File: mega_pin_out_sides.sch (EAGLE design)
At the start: 101 parts, among them T1 2N2222, T10 2N2222, T11 2N2222, T12 2N2222, T13 2N2222, T14 2N2222, T15 2N2222, T16 2N2222, T17 2N2222, T18 2N2222, T2 2N2222, T3 2N2222, T4 2N2222, T5 2N2222, T6 2N2222, T7 2N2222, T8 2N2222, T9 2N2222

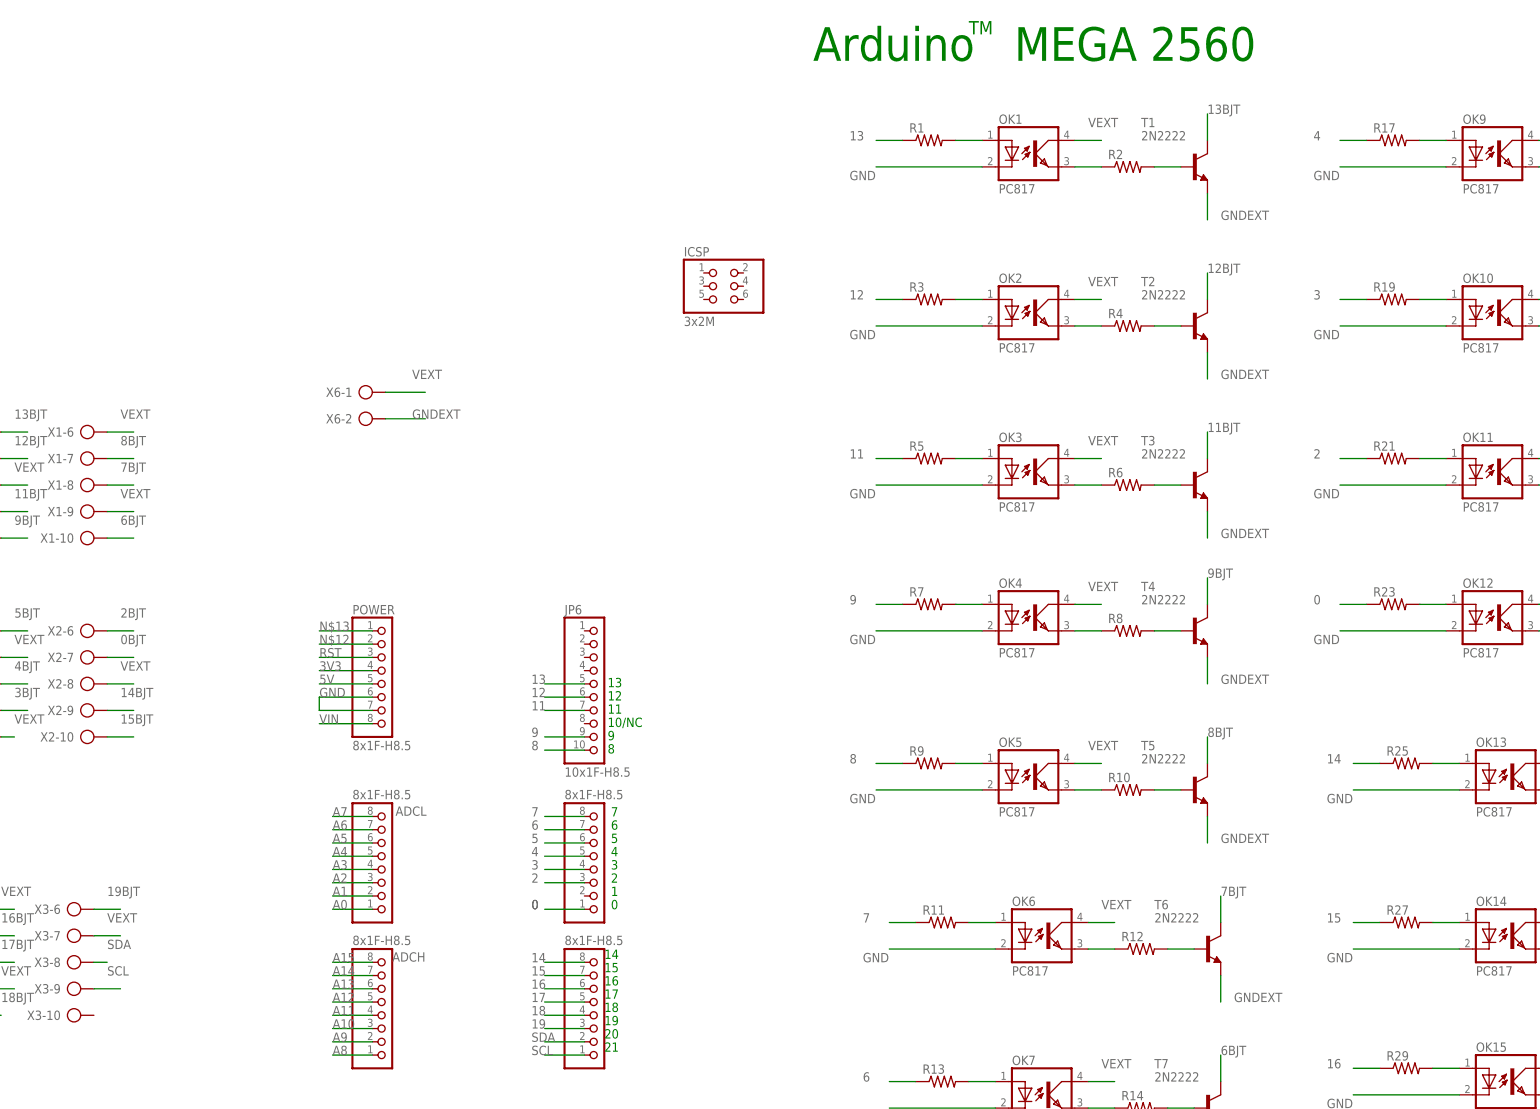
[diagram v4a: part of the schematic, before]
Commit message: [SIDES] Added header jumper pins for Flashing
- During Flashing or Reset Pin 13, 9 & 0 flashes several times and this will trigger the relays. A header jumper to be removed during flashing and after start up they are back again in place.
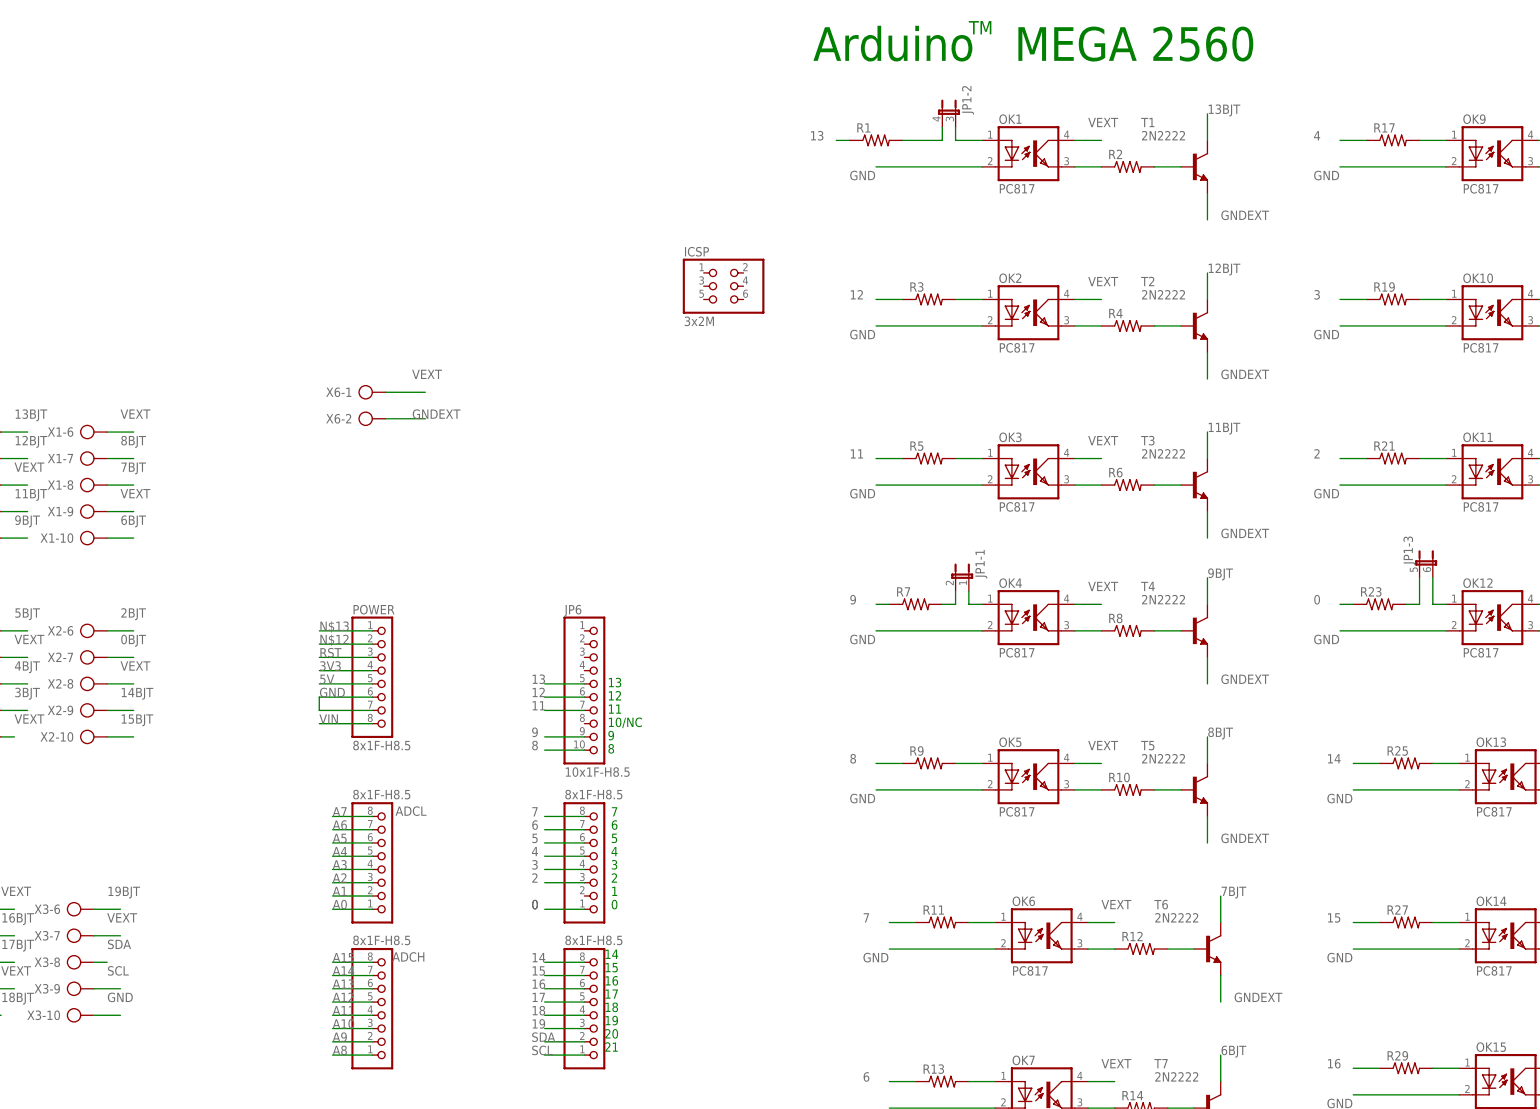
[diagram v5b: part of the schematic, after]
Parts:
- added JP1: (no value), jumper:JP3QE
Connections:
- new net N$10: JP1-3.2, OK12.A
- new net N$11: JP1-1.1, OK4.A
- new net N$9: JP1-2.1, OK1.A
- net GND: now also X3-10.KL
- net N$1: now also JP1-2.2; no longer OK1.A
- net N$19: now also JP1-1.2; no longer OK4.A
- net N$44: now also JP1-3.1; no longer OK12.A
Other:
- moved on the sheet: R1, R23, R7
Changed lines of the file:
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@@
 <part name="C15" library="adafruit" deviceset="CPOL-US" device="E2-4"/>
 <part name="C16" library="adafruit" deviceset="CPOL-US" device="E2-4"/>
+<part name="JP1" library="jumper" deviceset="JP3QE" device=""/>
 </parts>
 <sheets>
@@
 <instance part="X5" gate="-9" x="71.12" y="-121.92"/>
 <instance part="X5" gate="-10" x="76.2" y="-144.78"/>
-<instance part="R1" gate="G$1" x="127" y="165.1"/>
+<instance part="R1" gate="G$1" x="116.84" y="165.1"/>
 <instance part="OK1" gate="A" x="147.32" y="162.56"/>
 <instance part="R2" gate="G$1" x="165.1" y="160.02"/>
@@
 <instance part="R6" gate="G$1" x="165.1" y="99.06"/>
 <instance part="T3" gate="G$1" x="177.8" y="99.06"/>
-<instance part="R7" gate="G$1" x="127" y="76.2"/>
+<instance part="R7" gate="G$1" x="124.46" y="76.2"/>
 <instance part="OK4" gate="A" x="147.32" y="73.66"/>
 <instance part="R8" gate="G$1" x="165.1" y="71.12"/>
@@
 <instance part="R32" gate="G$1" x="256.54" y="-48.26"/>
 <instance part="T16" gate="G$1" x="269.24" y="-48.26"/>
-<instance part="R23" gate="G$1" x="215.9" y="76.2"/>
+<instance part="R23" gate="G$1" x="213.36" y="76.2"/>
 <instance part="OK12" gate="A" x="236.22" y="73.66"/>
 <instance part="R24" gate="G$1" x="254" y="71.12"/>
@@
 <instance part="C15" gate="G$1" x="83.82" y="-129.54"/>
 <instance part="C16" gate="G$1" x="83.82" y="-152.4"/>
+<instance part="JP1" gate="-1" x="134.62" y="81.28" rot="MR0"/>
+<instance part="JP1" gate="-2" x="132.08" y="170.18" rot="MR0"/>
+<instance part="JP1" gate="-3" x="220.98" y="83.82"/>
 </instances>
 <busses>
@@
 <segment>
 <pinref part="R1" gate="G$1" pin="2"/>
-<pinref part="OK1" gate="A" pin="A"/>
-<wire x1="132.08" y1="165.1" x2="137.16" y2="165.1" width="0.1524" layer="91"/>
+<wire x1="121.92" y1="165.1" x2="129.54" y2="165.1" width="0.1524" layer="91"/>
+<pinref part="JP1" gate="-2" pin="2"/>
+<wire x1="129.54" y1="165.1" x2="129.54" y2="167.64" width="0.1524" layer="91"/>
 </segment>
 </net>
@@
 <segment>
 <pinref part="R1" gate="G$1" pin="1"/>
-<wire x1="121.92" y1="165.1" x2="116.84" y2="165.1" width="0.1524" layer="91"/>
-<label x="111.76" y="165.1" size="1.778" layer="95"/>
+<wire x1="111.76" y1="165.1" x2="109.22" y2="165.1" width="0.1524" layer="91"/>
+<label x="104.14" y="165.1" size="1.778" layer="95"/>
 </segment>
 </net>
@@
 <label x="-96.52" y="-38.1" size="1.778" layer="95"/>
 </segment>
+<segment>
+<pinref part="X3" gate="-10" pin="KL"/>
+<wire x1="-33.02" y1="-2.54" x2="-27.94" y2="-2.54" width="0.1524" layer="91"/>
+<label x="-30.48" y="0" size="1.778" layer="95"/>
+</segment>
 </net>
 <net name="5V" class="0">
@@
 <segment>
 <pinref part="R7" gate="G$1" pin="2"/>
-<pinref part="OK4" gate="A" pin="A"/>
-<wire x1="132.08" y1="76.2" x2="137.16" y2="76.2" width="0.1524" layer="91"/>
+<wire x1="129.54" y1="76.2" x2="132.08" y2="76.2" width="0.1524" layer="91"/>
+<wire x1="132.08" y1="76.2" x2="132.08" y2="78.74" width="0.1524" layer="91"/>
+<pinref part="JP1" gate="-1" pin="2"/>
 </segment>
 </net>
@@
 <segment>
 <pinref part="R7" gate="G$1" pin="1"/>
-<wire x1="121.92" y1="76.2" x2="116.84" y2="76.2" width="0.1524" layer="91"/>
+<wire x1="119.38" y1="76.2" x2="116.84" y2="76.2" width="0.1524" layer="91"/>
 <label x="111.76" y="76.2" size="1.778" layer="95"/>
 </segment>
@@
 <segment>
 <pinref part="R23" gate="G$1" pin="2"/>
-<pinref part="OK12" gate="A" pin="A"/>
-<wire x1="220.98" y1="76.2" x2="226.06" y2="76.2" width="0.1524" layer="91"/>
+<wire x1="218.44" y1="76.2" x2="220.98" y2="76.2" width="0.1524" layer="91"/>
+<pinref part="JP1" gate="-3" pin="1"/>
+<wire x1="220.98" y1="81.28" x2="220.98" y2="76.2" width="0.1524" layer="91"/>
 </segment>
 </net>
@@
 <segment>
 <pinref part="R23" gate="G$1" pin="1"/>
-<wire x1="210.82" y1="76.2" x2="205.74" y2="76.2" width="0.1524" layer="91"/>
+<wire x1="208.28" y1="76.2" x2="205.74" y2="76.2" width="0.1524" layer="91"/>
 <label x="200.66" y="76.2" size="1.778" layer="95"/>
 </segment>
@@
 </segment>
 </net>
+<net name="N$10" class="0">
+<segment>
+<pinref part="JP1" gate="-3" pin="2"/>
+<wire x1="223.52" y1="81.28" x2="223.52" y2="76.2" width="0.1524" layer="91"/>
+<pinref part="OK12" gate="A" pin="A"/>
+<wire x1="223.52" y1="76.2" x2="226.06" y2="76.2" width="0.1524" layer="91"/>
+</segment>
+</net>
+<net name="N$9" class="0">
+<segment>
+<pinref part="JP1" gate="-2" pin="1"/>
+<pinref part="OK1" gate="A" pin="A"/>
+<wire x1="132.08" y1="167.64" x2="132.08" y2="165.1" width="0.1524" layer="91"/>
+<wire x1="132.08" y1="165.1" x2="137.16" y2="165.1" width="0.1524" layer="91"/>
+</segment>
+</net>
+<net name="N$11" class="0">
+<segment>
+<pinref part="JP1" gate="-1" pin="1"/>
+<pinref part="OK4" gate="A" pin="A"/>
+<wire x1="134.62" y1="78.74" x2="134.62" y2="76.2" width="0.1524" layer="91"/>
+<wire x1="134.62" y1="76.2" x2="137.16" y2="76.2" width="0.1524" layer="91"/>
+</segment>
+</net>
